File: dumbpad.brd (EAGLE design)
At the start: 97 x 78.5 mm, 44 parts

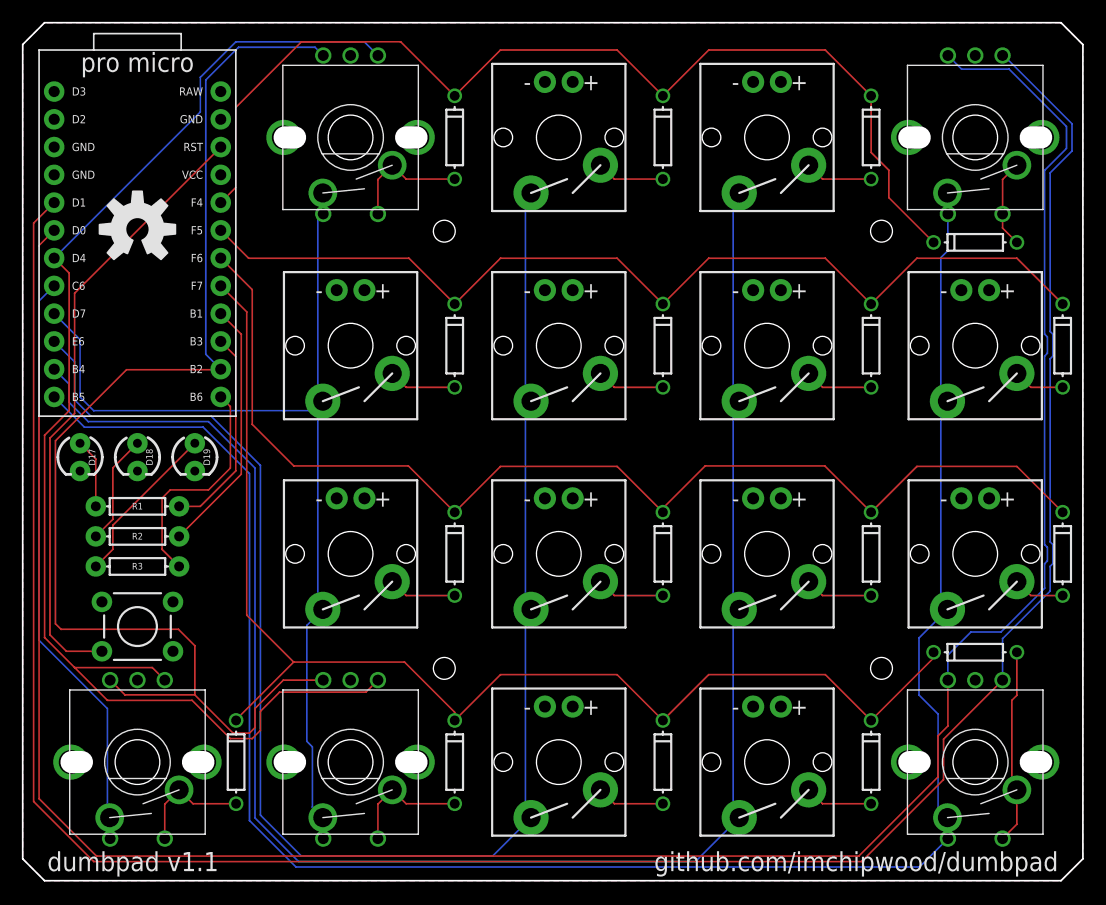
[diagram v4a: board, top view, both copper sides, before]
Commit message: long pads with mill
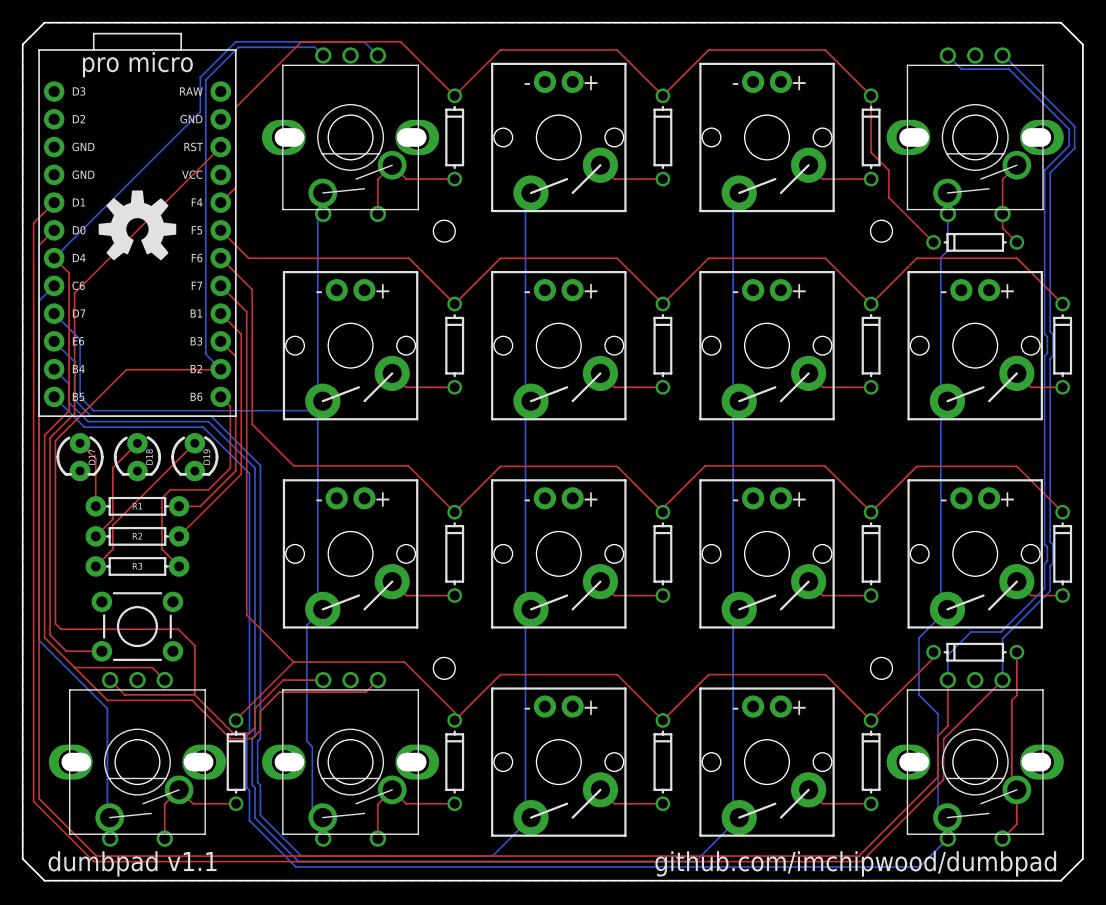
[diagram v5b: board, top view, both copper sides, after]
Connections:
- net COL0: now also RE_3_0.S2; no longer RE_3_0.S1_1
- net COL1: now also RE_0_1.S2, RE_3_1.S2; no longer RE_0_1.S1_1, RE_3_1.S1_1
- net COL4: now also RE_0_4.S2, RE_3_4.S2; no longer RE_0_4.S1_1, RE_3_4.S1_1
- net N$1: now also RE_0_4.S1; no longer RE_0_4.S2_1
- net N$11: now also RE_3_4.S1; no longer RE_3_4.S2_1
- net N$14: now also RE_3_1.S1; no longer RE_3_1.S2_1
- net N$20: now also RE_3_0.S1; no longer RE_3_0.S2_1
- net N$4: now also RE_0_1.S1; no longer RE_0_1.S2_1
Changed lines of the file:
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@@
 </class>
 </classes>
-<designrules name="oshpark-2layer">
+<designrules name="oshpark-2layer *">
 <description language="en">&lt;b&gt;OSH Park Design Rules&lt;/b&gt;
 &lt;p&gt;
@@
 <param name="psBottom" value="-1"/>
 <param name="psFirst" value="-1"/>
-<param name="psElongationLong" value="100"/>
+<param name="psElongationLong" value="25"/>
 <param name="psElongationOffset" value="100"/>
 <param name="mvStopFrame" value="1"/>
@@
 <signal name="N$1">
 <contactref element="D4" pad="A"/>
-<contactref element="RE_0_4" pad="S2_1"/>
+<contactref element="RE_0_4" pad="S1"/>
 <contactref element="RE_0_4" pad="D"/>
 <wire x1="90.96" y1="58.4" x2="89.65" y2="59.71" width="0.1524" layer="1"/>
@@
 <signal name="N$4">
 <contactref element="D1" pad="A"/>
-<contactref element="RE_0_1" pad="S2_1"/>
+<contactref element="RE_0_1" pad="S1"/>
 <contactref element="RE_0_1" pad="D"/>
 <wire x1="39.525" y1="64.19" x2="35.08" y2="64.19" width="0.1524" layer="1"/>
@@
 <signal name="N$11">
 <contactref element="D16" pad="A"/>
-<contactref element="RE_3_4" pad="S2_1"/>
+<contactref element="RE_3_4" pad="S1"/>
 <contactref element="RE_3_4" pad="D"/>
 <wire x1="90.96" y1="20.9" x2="90.96" y2="16.96" width="0.1524" layer="1"/>
@@
 <signal name="N$14">
 <contactref element="D13" pad="A"/>
-<contactref element="RE_3_1" pad="S2_1"/>
+<contactref element="RE_3_1" pad="S1"/>
 <contactref element="RE_3_1" pad="D"/>
 <wire x1="39.525" y1="7.04" x2="35.08" y2="7.04" width="0.1524" layer="1"/>
@@
 <wire x1="5.25" y1="44.25" x2="5.25" y2="49.51" width="0.1524" layer="16"/>
 <contactref element="RE_3_1" pad="E"/>
-<contactref element="RE_3_1" pad="S1_1"/>
+<contactref element="RE_3_1" pad="S2"/>
 <wire x1="26" y1="12.75" x2="26.5" y2="12.25" width="0.1524" layer="16"/>
 <wire x1="26" y1="23.36" x2="26" y2="12.75" width="0.1524" layer="16"/>
@@
 <wire x1="27.5" y1="5.73" x2="27.5" y2="3.85" width="0.1524" layer="16"/>
 <contactref element="RE_0_1" pad="E"/>
-<contactref element="RE_0_1" pad="S1_1"/>
+<contactref element="RE_0_1" pad="S2"/>
 <wire x1="27.46" y1="43.87" x2="27" y2="44.33" width="0.1524" layer="16"/>
 <wire x1="27" y1="60.5" x2="27.5" y2="61" width="0.1524" layer="16"/>
@@
 <wire x1="46" y1="44.38" x2="46" y2="62.41" width="0.1524" layer="16"/>
 <wire x1="46" y1="62.41" x2="46.51" y2="62.92" width="0.1524" layer="16"/>
-<wire x1="21.75" y1="38" x2="21.75" y2="6" width="0.1524" layer="16"/>
+<wire x1="21.75" y1="38" x2="21.75" y2="13" width="0.1524" layer="16"/>
+<wire x1="21.75" y1="13" x2="21.5" y2="12.75" width="0.1524" layer="16"/>
+<wire x1="21.5" y1="12.75" x2="21.5" y2="9" width="0.1524" layer="16"/>
+<wire x1="21.5" y1="9" x2="21.75" y2="8.75" width="0.1524" layer="16"/>
+<wire x1="21.75" y1="8.75" x2="21.75" y2="6" width="0.1524" layer="16"/>
 <wire x1="21.75" y1="6" x2="25.5" y2="2.25" width="0.1524" layer="16"/>
 <wire x1="21.75" y1="38" x2="17.25" y2="42.5" width="0.1524" layer="16"/>
@@
 <wire x1="25.25" y1="1.75" x2="61.54" y2="1.75" width="0.1524" layer="16"/>
 <wire x1="25.25" y1="1.75" x2="21.25" y2="5.75" width="0.1524" layer="16"/>
-<wire x1="21.25" y1="5.75" x2="21.25" y2="37.75" width="0.1524" layer="16"/>
+<wire x1="21.25" y1="5.75" x2="21.25" y2="8.5" width="0.1524" layer="16"/>
+<wire x1="21.25" y1="8.5" x2="21" y2="8.75" width="0.1524" layer="16"/>
+<wire x1="21" y1="8.75" x2="21" y2="13" width="0.1524" layer="16"/>
+<wire x1="21" y1="13" x2="21.25" y2="13.25" width="0.1524" layer="16"/>
+<wire x1="21.25" y1="13.25" x2="21.25" y2="37.75" width="0.1524" layer="16"/>
 <wire x1="21.25" y1="37.75" x2="17" y2="42" width="0.1524" layer="16"/>
 <wire x1="61.54" y1="1.75" x2="65.56" y2="5.77" width="0.1524" layer="16"/>
@@
 <wire x1="84" y1="25.43" x2="84" y2="43.26" width="0.1524" layer="16"/>
 <wire x1="84" y1="43.26" x2="84.61" y2="43.87" width="0.1524" layer="16"/>
-<wire x1="20.75" y1="5.5" x2="25" y2="1.25" width="0.1524" layer="16"/>
-<wire x1="20.75" y1="5.5" x2="20.75" y2="37.25" width="0.1524" layer="16"/>
+<wire x1="25" y1="1.25" x2="20.75" y2="5.5" width="0.1524" layer="16"/>
+<wire x1="20.75" y1="5.5" x2="20.75" y2="8.25" width="0.1524" layer="16"/>
+<wire x1="20.75" y1="8.25" x2="20.5" y2="8.5" width="0.1524" layer="16"/>
+<wire x1="20.5" y1="8.5" x2="20.5" y2="13.25" width="0.1524" layer="16"/>
+<wire x1="20.5" y1="13.25" x2="20.75" y2="13.5" width="0.1524" layer="16"/>
+<wire x1="20.75" y1="13.5" x2="20.75" y2="37.25" width="0.1524" layer="16"/>
 <wire x1="20.75" y1="37.25" x2="16.5" y2="41.5" width="0.1524" layer="16"/>
 <wire x1="5.64" y1="41.5" x2="2.88" y2="44.26" width="0.1524" layer="16"/>
 <wire x1="16.5" y1="41.5" x2="5.64" y2="41.5" width="0.1524" layer="16"/>
 <contactref element="RE_3_4" pad="E"/>
-<contactref element="RE_3_4" pad="S1_1"/>
+<contactref element="RE_3_4" pad="S2"/>
 <wire x1="82.05" y1="1.25" x2="84.65" y2="3.85" width="0.1524" layer="16"/>
 <wire x1="25" y1="1.25" x2="82.05" y2="1.25" width="0.1524" layer="16"/>
@@
 <wire x1="84.61" y1="3.89" x2="84.65" y2="3.85" width="0.1524" layer="16"/>
 <contactref element="RE_0_4" pad="E"/>
-<contactref element="RE_0_4" pad="S1_1"/>
+<contactref element="RE_0_4" pad="S2"/>
 <wire x1="84.65" y1="61" x2="84.65" y2="62.88" width="0.1524" layer="16"/>
 <wire x1="84.65" y1="62.88" x2="84.61" y2="62.92" width="0.1524" layer="16"/>
@@
 <wire x1="89.75" y1="75.5" x2="89.65" y2="75.5" width="0.1524" layer="16"/>
 <wire x1="94" y1="26.5" x2="89.65" y2="22.15" width="0.1524" layer="16"/>
-<wire x1="96" y1="66.75" x2="94" y2="64.75" width="0.1524" layer="16"/>
-<wire x1="96" y1="66.75" x2="96" y2="69.25" width="0.1524" layer="16"/>
-<wire x1="96" y1="69.25" x2="89.75" y2="75.5" width="0.1524" layer="16"/>
+<wire x1="96.25" y1="67" x2="94" y2="64.75" width="0.1524" layer="16"/>
+<wire x1="96.25" y1="67" x2="96.25" y2="69" width="0.1524" layer="16"/>
+<wire x1="96.25" y1="69" x2="89.75" y2="75.5" width="0.1524" layer="16"/>
 <wire x1="94" y1="50.25" x2="94.25" y2="50" width="0.1524" layer="16"/>
 <wire x1="94.25" y1="50" x2="94.25" y2="48" width="0.1524" layer="16"/>
@@
 <wire x1="86.75" y1="22.75" x2="89.5" y2="22.75" width="0.1524" layer="16"/>
 <wire x1="89.5" y1="22.75" x2="93.5" y2="26.75" width="0.1524" layer="16"/>
-<wire x1="95.5" y1="69" x2="90.25" y2="74.25" width="0.1524" layer="16"/>
+<wire x1="95.75" y1="68.75" x2="90.25" y2="74.25" width="0.1524" layer="16"/>
 <wire x1="85.9" y1="74.25" x2="84.65" y2="75.5" width="0.1524" layer="16"/>
-<wire x1="93.5" y1="65" x2="95.5" y2="67" width="0.1524" layer="16"/>
-<wire x1="95.5" y1="67" x2="95.5" y2="69" width="0.1524" layer="16"/>
+<wire x1="93.5" y1="65" x2="95.75" y2="67.25" width="0.1524" layer="16"/>
+<wire x1="95.75" y1="67.25" x2="95.75" y2="68.75" width="0.1524" layer="16"/>
 <wire x1="90.25" y1="74.25" x2="85.9" y2="74.25" width="0.1524" layer="16"/>
 <wire x1="93.5" y1="29" x2="93.75" y2="29.25" width="0.1524" layer="16"/>
@@
 <contactref element="B1" pad="8"/>
 <contactref element="RE_3_0" pad="E"/>
-<contactref element="RE_3_0" pad="S1_1"/>
+<contactref element="RE_3_0" pad="S2"/>
 <wire x1="8" y1="3.85" x2="7.96" y2="3.89" width="0.1524" layer="16"/>
 <wire x1="7.96" y1="3.89" x2="7.96" y2="5.77" width="0.1524" layer="16"/>
@@
 </signal>
 <signal name="N$20">
-<contactref element="RE_3_0" pad="S2_1"/>
+<contactref element="RE_3_0" pad="S1"/>
 <contactref element="RE_3_0" pad="D"/>
 <contactref element="D20" pad="A"/>

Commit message: rerouted some stuff
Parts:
- moved D17 0.45 mm to (4.80, 38.8)
- moved D18 0.45 mm to (10.1, 38.8)
- moved D19 0.45 mm to (15.3, 38.8)
- moved R1 0.45 mm to (10.1, 34.2)
- moved R2 0.45 mm to (10.1, 31.5)
- moved R3 0.45 mm to (10.1, 28.8)
- moved RE_3_0 0.45 mm to (10.1, 10.8)
- moved S17 0.45 mm to (10.1, 23.2)
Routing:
- net ENCODER1_L0: track 218.6 -> 157.3 mm
- net ENCODER1_L1: track 220.1 -> 161.2 mm
- net ENCODER0_L0: track 116.5 -> 103.4 mm
- net ENCODER0_L1: track 122.7 -> 109.9 mm
- net ROW0: track 94.7 -> 82.2 mm
- net ROW1: track 90.2 -> 79.8 mm
- net ROW2: track 104.4 -> 96.4 mm
- net ROW3: track 115.7 -> 120.8 mm
- net COL3: track 161.5 -> 159.9 mm
- net COL2: track 144.0 -> 142.5 mm
- net COL4: track 181.8 -> 180.5 mm
- net COL1: track 92.1 -> 91.6 mm
